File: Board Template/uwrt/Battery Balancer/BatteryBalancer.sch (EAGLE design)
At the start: 18 parts, among them P1 39-30-06, P2 39-30-06, P3 39-30-06, P4 39-30-08, P5 39-30-08, P6 39-30-02

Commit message: Changed Battery Balancer
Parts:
- removed P6: 39-30-02, con-molex-mini-fit:39-30-02
- added C1: (no value), rcl:C-EUC0603
- added C2: (no value), rcl:CPOL-USE2-4
- added R1, R2, R3, R4: 100K, rcl:R-US_R0603
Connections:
- new net GNDA: C1.2, C2.-, R3.2, R4.2, U$12.GND
- new net N$7: R1.2, R3.1, U$12.A0
- new net N$8: R1.1, R2.1, R2.2, R4.1, U$12.A1, U$12.V+
- net +3V3: now also C1.1, C2.+, U$12.VREF
- net KILL_SWITCH: no longer P6.1

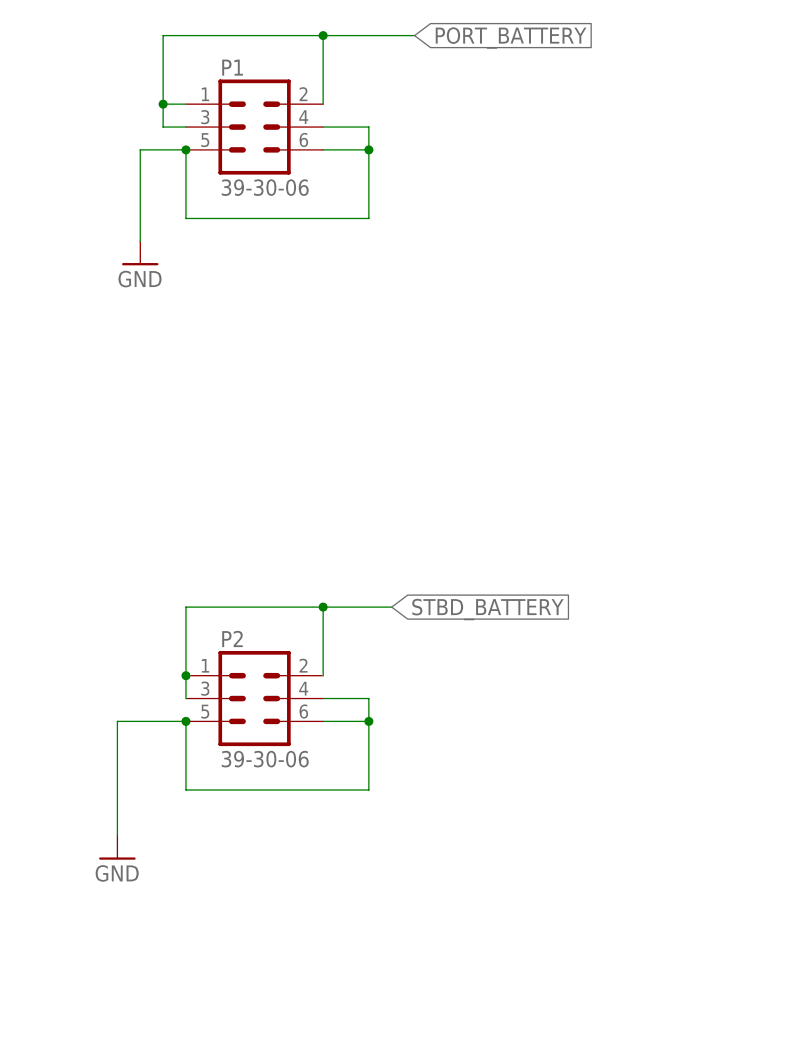
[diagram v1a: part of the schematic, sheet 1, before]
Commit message: Finished parts for Battery Balancer
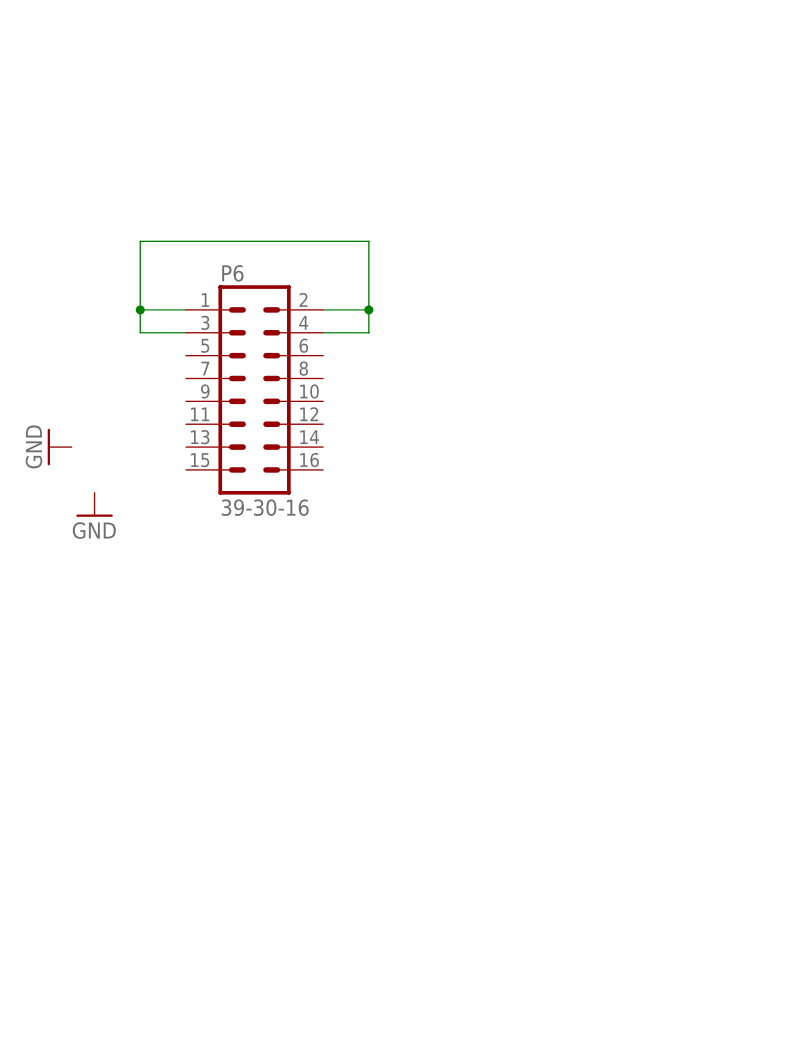
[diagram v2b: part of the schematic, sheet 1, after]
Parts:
- removed P1, P2: 39-30-06, con-molex-mini-fit:39-30-06
- added P6: 39-30-16, con-molex-mini-fit:39-30-16
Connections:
- new net N$6: P6.1, P6.2, P6.3, P6.4
- net GND: no longer P1.4, P1.5, P1.6, P2.4, P2.5, P2.6
- net PORT_BATTERY: no longer P1.1, P1.2, P1.3
- net STBD_BATTERY: no longer P2.1, P2.2, P2.3
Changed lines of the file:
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@@
 <part name="+3V1" library="supply1" library_urn="urn:adsk.eagle:library:371" deviceset="+3V3" device=""/>
 <part name="FRAME1" library="frames" library_urn="urn:adsk.eagle:library:229" deviceset="A3L-LOC" device="" value="a"/>
-<part name="P1" library="con-molex-mini-fit" deviceset="39-30-?06?" device=""/>
-<part name="P2" library="con-molex-mini-fit" deviceset="39-30-?06?" device=""/>
 <part name="P3" library="con-molex-mini-fit" deviceset="39-30-?06?" device=""/>
 <part name="P4" library="con-molex-mini-fit" deviceset="39-30-?08?" device=""/>
@@
 <part name="+3V6" library="supply1" library_urn="urn:adsk.eagle:library:371" deviceset="+3V3" device=""/>
 <part name="C1" library="rcl" library_urn="urn:adsk.eagle:library:334" deviceset="C-EU" device="C0603" package3d_urn="urn:adsk.eagle:package:23616/2"/>
+<part name="P6" library="con-molex-mini-fit" deviceset="39-30-?16?" device=""/>
 </parts>
 <sheets>
@@
 <attribute name="SHEET" x="357.680259375" y="4.9784" size="2.54" layer="94"/>
 </instance>
-<instance part="P1" gate="G$1" x="35.56" y="223.52">
-<attribute name="NAME" x="31.75" y="229.235" size="1.778" layer="95"/>
-<attribute name="VALUE" x="31.75" y="215.9" size="1.778" layer="95"/>
-</instance>
-<instance part="P2" gate="G$1" x="35.56" y="160.02">
-<attribute name="NAME" x="31.75" y="165.735" size="1.778" layer="95"/>
-<attribute name="VALUE" x="31.75" y="152.4" size="1.778" layer="95"/>
-</instance>
 <instance part="P3" gate="G$1" x="340.36" y="165.1" rot="MR0">
 <attribute name="NAME" x="344.17" y="170.815" size="1.778" layer="95" rot="MR0"/>
@@
 <attribute name="VALUE" x="346.71" y="101.6" size="1.778" layer="95" rot="MR0"/>
 </instance>
-<instance part="GND2" gate="1" x="20.32" y="142.24">
-<attribute name="VALUE" x="17.78" y="139.7" size="1.778" layer="96"/>
+<instance part="GND2" gate="1" x="12.7" y="187.96" rot="R270">
+<attribute name="VALUE" x="10.16" y="190.5" size="1.778" layer="96" rot="R270"/>
 </instance>
-<instance part="GND3" gate="1" x="22.86" y="208.28">
-<attribute name="VALUE" x="20.32" y="205.74" size="1.778" layer="96"/>
+<instance part="GND3" gate="1" x="17.78" y="180.34">
+<attribute name="VALUE" x="15.24" y="177.8" size="1.778" layer="96"/>
 </instance>
 <instance part="GND4" gate="1" x="355.6" y="96.52">
@@
 <instance part="GND6" gate="1" x="360.68" y="152.4">
 <attribute name="VALUE" x="358.14" y="149.86" size="1.778" layer="96"/>
+</instance>
+<instance part="P6" gate="G$1" x="35.56" y="193.04">
+<attribute name="NAME" x="31.75" y="206.375" size="1.778" layer="95"/>
+<attribute name="VALUE" x="31.75" y="180.34" size="1.778" layer="95"/>
 </instance>
 </instances>
@@
 <wire x1="358.14" y1="60.96" x2="350.52" y2="60.96" width="0.1524" layer="91"/>
 </segment>
-<segment>
-<pinref part="P2" gate="G$1" pin="4"/>
-<wire x1="43.18" y1="160.02" x2="48.26" y2="160.02" width="0.1524" layer="91"/>
-<pinref part="P2" gate="G$1" pin="6"/>
-<wire x1="48.26" y1="160.02" x2="48.26" y2="157.48" width="0.1524" layer="91"/>
-<wire x1="48.26" y1="157.48" x2="43.18" y2="157.48" width="0.1524" layer="91"/>
-<wire x1="48.26" y1="157.48" x2="48.26" y2="149.86" width="0.1524" layer="91"/>
-<wire x1="48.26" y1="149.86" x2="27.94" y2="149.86" width="0.1524" layer="91"/>
-<junction x="48.26" y="157.48"/>
-<pinref part="P2" gate="G$1" pin="5"/>
-<wire x1="27.94" y1="149.86" x2="27.94" y2="157.48" width="0.1524" layer="91"/>
-<wire x1="27.94" y1="157.48" x2="20.32" y2="157.48" width="0.1524" layer="91"/>
-<junction x="27.94" y="157.48"/>
-<pinref part="GND2" gate="1" pin="GND"/>
-<wire x1="20.32" y1="157.48" x2="20.32" y2="144.78" width="0.1524" layer="91"/>
-</segment>
-<segment>
-<pinref part="P1" gate="G$1" pin="6"/>
-<wire x1="48.26" y1="220.98" x2="43.18" y2="220.98" width="0.1524" layer="91"/>
-<wire x1="48.26" y1="220.98" x2="48.26" y2="213.36" width="0.1524" layer="91"/>
-<wire x1="48.26" y1="213.36" x2="27.94" y2="213.36" width="0.1524" layer="91"/>
-<pinref part="P1" gate="G$1" pin="5"/>
-<wire x1="27.94" y1="213.36" x2="27.94" y2="220.98" width="0.1524" layer="91"/>
-<pinref part="P1" gate="G$1" pin="4"/>
-<wire x1="43.18" y1="223.52" x2="48.26" y2="223.52" width="0.1524" layer="91"/>
-<wire x1="48.26" y1="223.52" x2="48.26" y2="220.98" width="0.1524" layer="91"/>
-<junction x="48.26" y="220.98"/>
-<wire x1="27.94" y1="220.98" x2="22.86" y2="220.98" width="0.1524" layer="91"/>
-<junction x="27.94" y="220.98"/>
-<pinref part="GND3" gate="1" pin="GND"/>
-<wire x1="22.86" y1="220.98" x2="22.86" y2="210.82" width="0.1524" layer="91"/>
-</segment>
-</net>
-<net name="STBD_BATTERY" class="0">
-<segment>
-<pinref part="P2" gate="G$1" pin="2"/>
-<wire x1="43.18" y1="162.56" x2="43.18" y2="170.18" width="0.1524" layer="91"/>
-<wire x1="43.18" y1="170.18" x2="27.94" y2="170.18" width="0.1524" layer="91"/>
-<pinref part="P2" gate="G$1" pin="1"/>
-<wire x1="27.94" y1="170.18" x2="27.94" y2="162.56" width="0.1524" layer="91"/>
-<pinref part="P2" gate="G$1" pin="3"/>
-<wire x1="27.94" y1="160.02" x2="27.94" y2="162.56" width="0.1524" layer="91"/>
-<junction x="27.94" y="162.56"/>
-<wire x1="43.18" y1="170.18" x2="50.8" y2="170.18" width="0.1524" layer="91"/>
-<junction x="43.18" y="170.18"/>
-<label x="50.8" y="170.18" size="1.778" layer="95" xref="yes"/>
-</segment>
-</net>
-<net name="PORT_BATTERY" class="0">
-<segment>
-<pinref part="P1" gate="G$1" pin="3"/>
-<wire x1="27.94" y1="223.52" x2="25.4" y2="223.52" width="0.1524" layer="91"/>
-<wire x1="25.4" y1="223.52" x2="25.4" y2="226.06" width="0.1524" layer="91"/>
-<pinref part="P1" gate="G$1" pin="2"/>
-<wire x1="25.4" y1="226.06" x2="25.4" y2="233.68" width="0.1524" layer="91"/>
-<wire x1="25.4" y1="233.68" x2="43.18" y2="233.68" width="0.1524" layer="91"/>
-<wire x1="43.18" y1="233.68" x2="43.18" y2="226.06" width="0.1524" layer="91"/>
-<pinref part="P1" gate="G$1" pin="1"/>
-<wire x1="27.94" y1="226.06" x2="25.4" y2="226.06" width="0.1524" layer="91"/>
-<junction x="25.4" y="226.06"/>
-<wire x1="43.18" y1="233.68" x2="53.34" y2="233.68" width="0.1524" layer="91"/>
-<junction x="43.18" y="233.68"/>
-<label x="53.34" y="233.68" size="1.778" layer="95" xref="yes"/>
-</segment>
 </net>
 <net name="BALANCED_OUT" class="0">
@@
 </segment>
 </net>
+<net name="N$6" class="0">
+<segment>
+<pinref part="P6" gate="G$1" pin="3"/>
+<wire x1="27.94" y1="200.66" x2="22.86" y2="200.66" width="0.1524" layer="91"/>
+<pinref part="P6" gate="G$1" pin="1"/>
+<wire x1="27.94" y1="203.2" x2="22.86" y2="203.2" width="0.1524" layer="91"/>
+<wire x1="22.86" y1="203.2" x2="22.86" y2="210.82" width="0.1524" layer="91"/>
+<wire x1="22.86" y1="210.82" x2="48.26" y2="210.82" width="0.1524" layer="91"/>
+<wire x1="48.26" y1="210.82" x2="48.26" y2="203.2" width="0.1524" layer="91"/>
+<pinref part="P6" gate="G$1" pin="2"/>
+<wire x1="48.26" y1="203.2" x2="43.18" y2="203.2" width="0.1524" layer="91"/>
+<pinref part="P6" gate="G$1" pin="4"/>
+<wire x1="43.18" y1="200.66" x2="48.26" y2="200.66" width="0.1524" layer="91"/>
+<wire x1="48.26" y1="200.66" x2="48.26" y2="203.2" width="0.1524" layer="91"/>
+<junction x="48.26" y="203.2"/>
+<wire x1="22.86" y1="200.66" x2="22.86" y2="203.2" width="0.1524" layer="91"/>
+<junction x="22.86" y="203.2"/>
+</segment>
+</net>

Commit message: Battery Balancer Update
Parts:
- removed P3: 39-30-06, con-molex-mini-fit:39-30-06
- removed P4, P5: 39-30-08, con-molex-mini-fit:39-30-08
- added P1: 39-30-14, con-molex-mini-fit:39-30-14
- added P2: 39-30-06, con-molex-mini-fit:39-30-06
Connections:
- removed net MOTOR_POWER1: P5.1, P5.2, P5.3, P5.4, U$8.LOAD-, U$9.LOAD-
- removed net N$6: P6.1, P6.2, P6.3, P6.4
- new net MOTOR_POWER: P1.1, P1.2, P1.3, P1.4, P1.5, P1.6, P1.7, U$8.LOAD-, U$9.LOAD-
- net BALANCED_OUT: now also P2.1, P2.2, P2.3; no longer P3.1, P3.2, P3.3
- net GND: now also P1.10, P1.11, P1.12, P1.13, P1.14, P1.8, P1.9, P2.4, P2.5, P2.6, P6.10, P6.11, P6.12, P6.13, P6.14, P6.15, P6.16, P6.9; no longer P3.4, P3.5, P3.6, P4.5, P4.6, P4.7, P4.8, P5.5, P5.6, P5.7, P5.8
- net MOTOR_POWER2: no longer P4.1, P4.2, P4.3, P4.4
- net PORT_BATTERY: now also P6.5, P6.6, P6.7, P6.8
- net STBD_BATTERY: now also P6.1, P6.2, P6.3, P6.4
